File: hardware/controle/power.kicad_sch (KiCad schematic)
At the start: 21 parts, among them J9 Barrel_Jack, U4 TPS54228, U5 NCP718xSN330

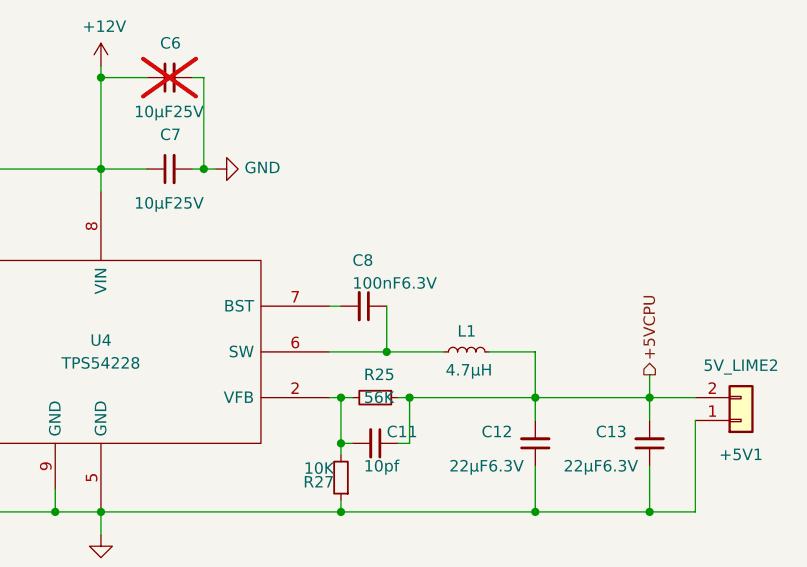
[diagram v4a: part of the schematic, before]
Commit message: hardware/controle: update some component values and P/N
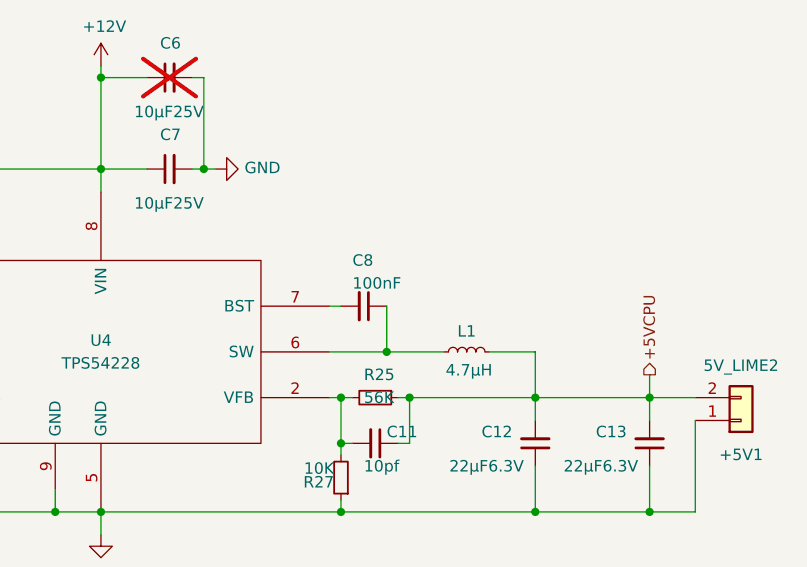
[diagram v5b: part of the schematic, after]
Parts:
- C8: value 100nF6.3V -> 100nF; P/N MC0603B104K250CT (stock) -> CC0805KKX7RYBB104
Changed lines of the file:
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@@
 			)
 		)
-		(property "Value" "100nF6.3V"
+		(property "Value" "100nF"
 			(at 146.05 74.93 90)
 			(effects
@@
 			)
 		)
-		(property "P/N" "MC0603B104K250CT (stock)"
+		(property "P/N" "CC0805KKX7RYBB104"
 			(at 179.07 27.94 0)
 			(effects

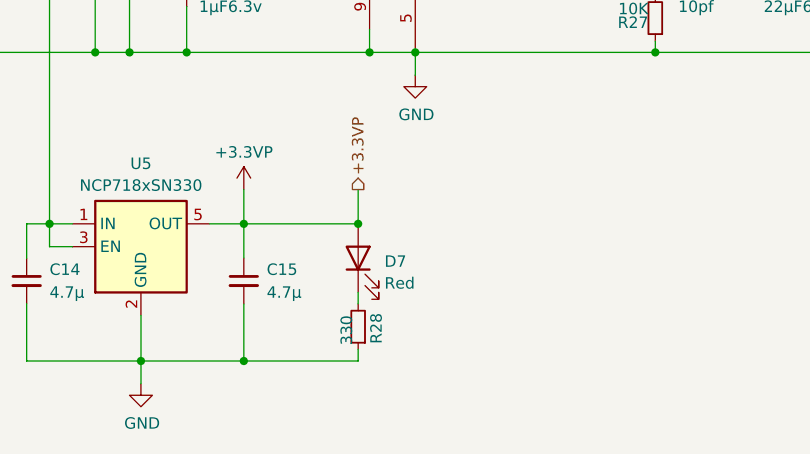
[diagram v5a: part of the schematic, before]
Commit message: hardware/controle: fix LED value
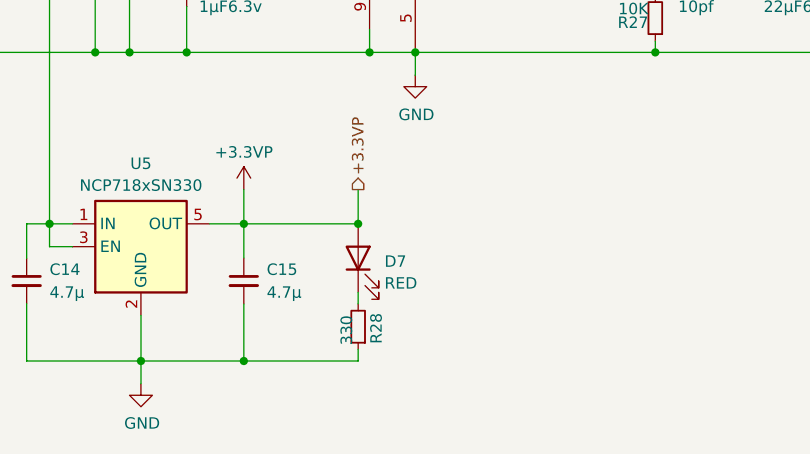
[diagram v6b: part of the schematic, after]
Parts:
- D7: value Red -> RED
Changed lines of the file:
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@@
 			)
 		)
-		(property "Value" "Red"
+		(property "Value" "RED"
 			(at 114.681 125.9896 90)
 			(effects

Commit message: hardware/controle: update P/N fields
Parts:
- C10: P/N CGA3E1X7R1V105K080AC (stock) -> CGA3E1X7R1V105K080AC
- C12, C13: P/N C3225X5R1A226M230AA/CL31A226KAHNNN (stock) -> C3225X5R1A226M230AA/CL31A226KAHNNN
- C14, C15: P/N CL21A475KPFNNNE -> 08053C475KAT2A
- C6, C7: P/N C3225X5R1E106K250AA (stock) -> GRM21BC8YA106KE11L
- C9: P/N GRM188R71H682KA01D (stock) -> C0603C682K5R
- R24, R25, R26: P/N stock -> MCWR08X5602FTL
- R27: P/N stock -> MCWR08X1002FTL
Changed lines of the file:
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@@
 			)
 		)
-		(property "P/N" "CGA3E1X7R1V105K080AC (stock)"
+		(property "P/N" "CGA3E1X7R1V105K080AC"
 			(at 92.71 92.71 0)
 			(effects
@@
 			)
 		)
-		(property "P/N" "C3225X5R1E106K250AA (stock)"
+		(property "P/N" "GRM21BC8YA106KE11L"
 			(at 83.82 76.2 0)
 			(effects
@@
 			)
 		)
-		(property "P/N" "stock"
+		(property "P/N" "MCWR08X5602FTL"
 			(at 148.59 87.63 0)
 			(effects
@@
 			)
 		)
-		(property "P/N" "C3225X5R1E106K250AA (stock)"
+		(property "P/N" "GRM21BC8YA106KE11L"
 			(at 83.82 86.36 0)
 			(effects
@@
 			)
 		)
-		(property "P/N" "stock"
+		(property "P/N" "MCWR08X1002FTL"
 			(at 144.78 96.52 0)
 			(effects
@@
 			)
 		)
-		(property "P/N" "C3225X5R1A226M230AA/CL31A226KAHNNN (stock)"
+		(property "P/N" "C3225X5R1A226M230AA/CL31A226KAHNNN"
 			(at 250.19 109.22 0)
 			(effects
@@
 			)
 		)
-		(property "P/N" "CL21A475KPFNNNE"
+		(property "P/N" "08053C475KAT2A"
 			(at 74.93 125.73 0)
 			(effects
@@
 			)
 		)
-		(property "P/N" "stock"
+		(property "P/N" "MCWR08X5602FTL"
 			(at 86.36 72.39 90)
 			(effects
@@
 			)
 		)
-		(property "P/N" "stock"
+		(property "P/N" "MCWR08X5602FTL"
 			(at 86.36 91.44 90)
 			(effects
@@
 			)
 		)
-		(property "P/N" "CL21A475KPFNNNE"
+		(property "P/N" "08053C475KAT2A"
 			(at 99.06 125.73 0)
 			(effects
@@
 			)
 		)
-		(property "P/N" "GRM188R71H682KA01D (stock)"
+		(property "P/N" "C0603C682K5R"
 			(at 100.33 54.61 0)
 			(effects
@@
 			)
 		)
-		(property "P/N" "C3225X5R1A226M230AA/CL31A226KAHNNN (stock)"
+		(property "P/N" "C3225X5R1A226M230AA/CL31A226KAHNNN"
 			(at 224.79 109.22 0)
 			(effects

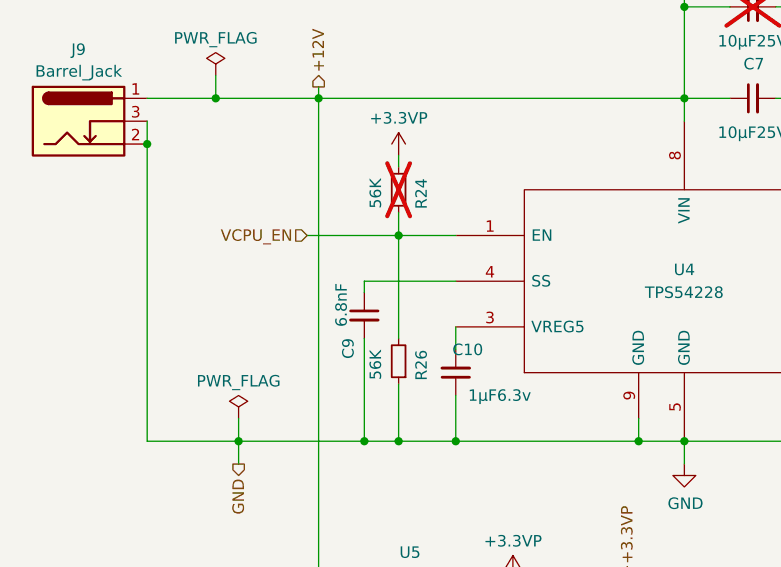
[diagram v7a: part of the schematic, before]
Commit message: rdware/controle: move back some resistors to 47k to match our stock
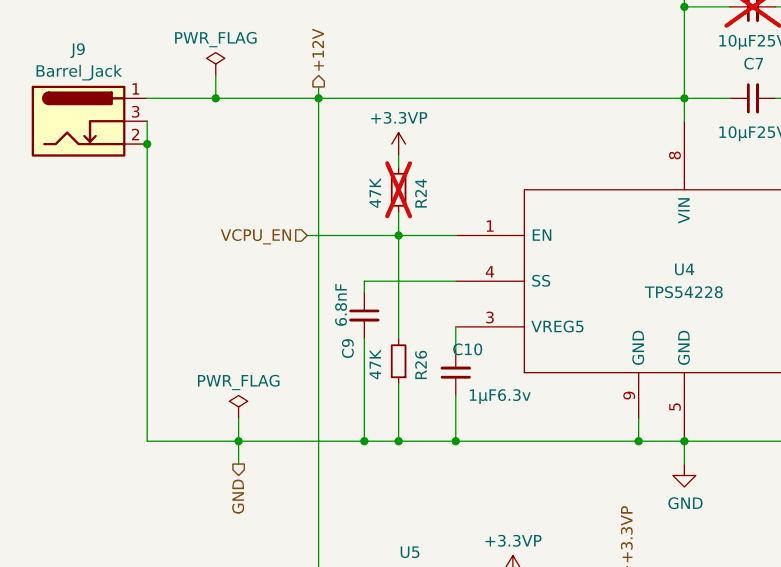
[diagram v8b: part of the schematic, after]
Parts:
- R24, R26: value 56K -> 47K; P/N MCWR08X5602FTL -> MCWR08X4702FTL
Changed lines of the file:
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@@
 			)
 		)
-		(property "Value" "56K"
+		(property "Value" "47K"
 			(at 83.82 71.12 90)
 			(effects
@@
 			)
 		)
-		(property "P/N" "MCWR08X5602FTL"
+		(property "P/N" "MCWR08X4702FTL"
 			(at 86.36 72.39 90)
 			(effects
@@
 			)
 		)
-		(property "Value" "56K"
+		(property "Value" "47K"
 			(at 83.82 90.17 90)
 			(effects
@@
 			)
 		)
-		(property "P/N" "MCWR08X5602FTL"
+		(property "P/N" "MCWR08X4702FTL"
 			(at 86.36 91.44 90)
 			(effects
